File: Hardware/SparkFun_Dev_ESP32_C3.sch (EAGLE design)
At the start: 35 parts, among them J1 USB Female Type C Connector, J4 QWIIC_RIGHT_ANGLE, U1 ESP32-C3, U2 RT9080-33GJ5, U3 WS2812-2020, Y1 40MHZ

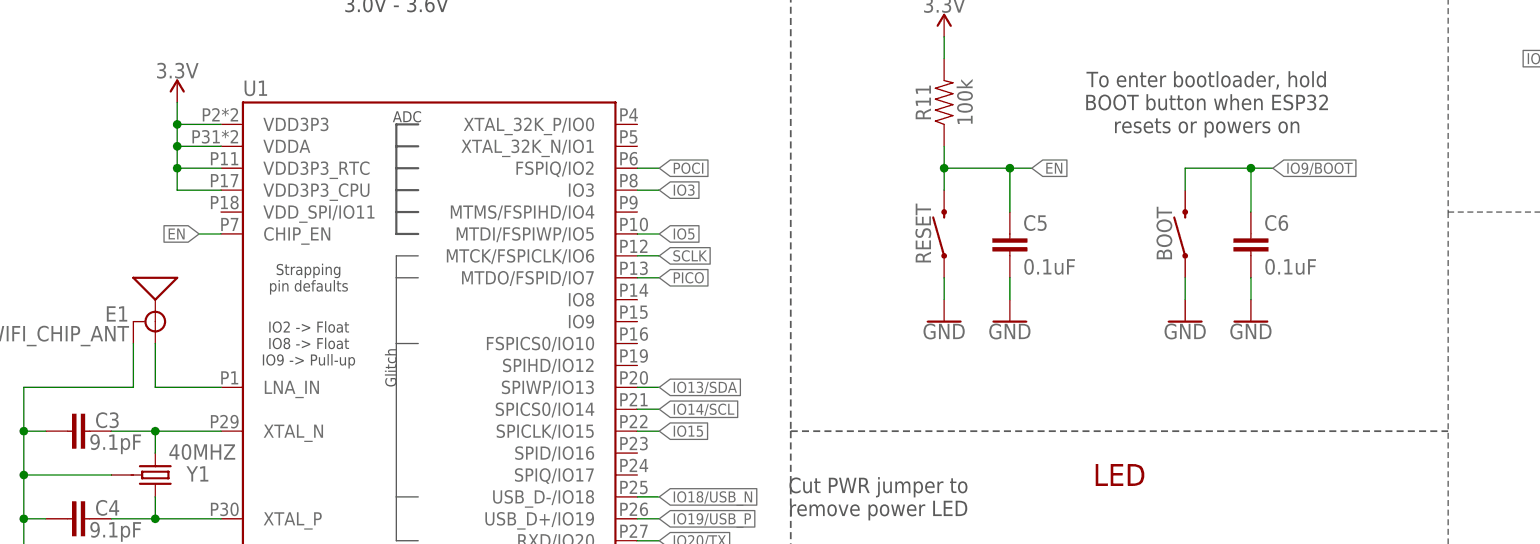
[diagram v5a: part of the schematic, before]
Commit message: Moves the parts into position
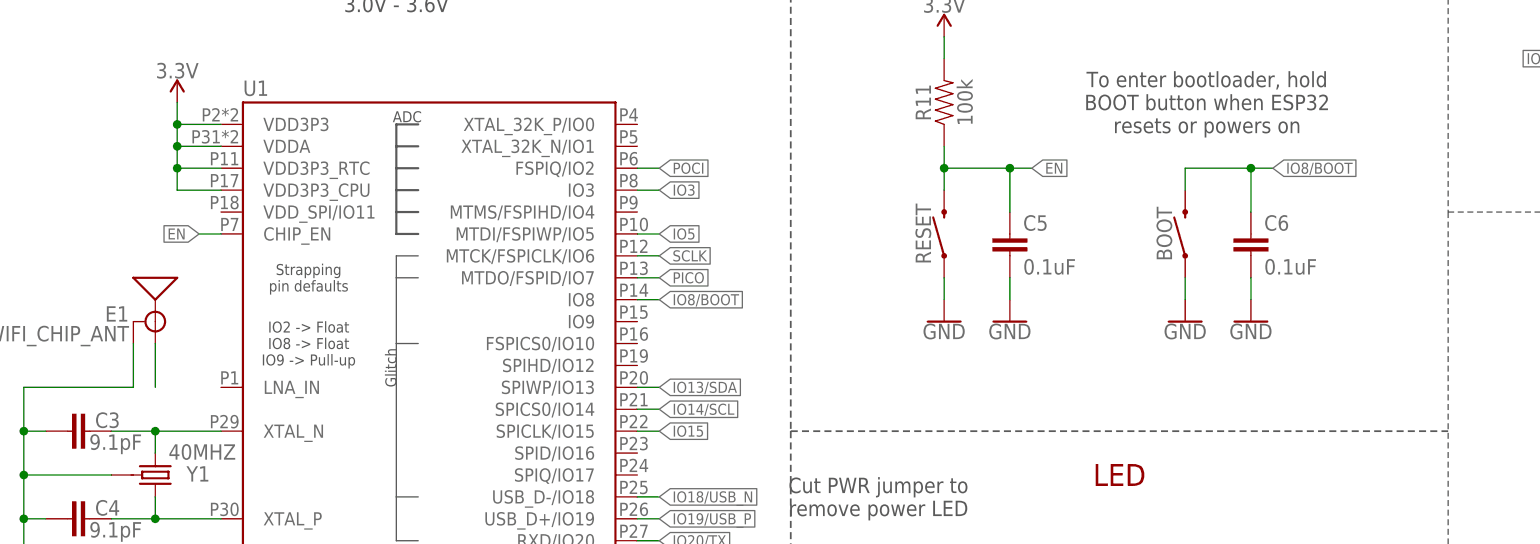
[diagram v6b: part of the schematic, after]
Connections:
- removed net IO9/BOOT: BOOT.2, C6.1
- removed net N$11: E1.SIGNAL, U1.LNA_IN
- new net ANT: E1.SIGNAL
- new net IO8/BOOT: BOOT.2, C6.1, U1.IO8
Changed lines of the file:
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@@
 </segment>
 </net>
-<net name="IO9/BOOT" class="0">
+<net name="IO8/BOOT" class="0">
 <segment>
 <pinref part="C6" gate="G$1" pin="1"/>
@@
 <junction x="533.4" y="129.54"/>
 <label x="535.94" y="129.54" size="1.27" layer="95" font="vector" xref="yes"/>
+</segment>
+<segment>
+<pinref part="U1" gate="G$1" pin="IO8"/>
+<wire x1="464.82" y1="114.3" x2="462.28" y2="114.3" width="0.1524" layer="91"/>
+<label x="464.82" y="114.3" size="1.27" layer="95" font="vector" xref="yes"/>
 </segment>
 </net>
@@
 </segment>
 </net>
-<net name="N$11" class="0">
+<net name="ANT" class="0">
 <segment>
 <wire x1="406.4" y1="104.14" x2="406.4" y2="109.22" width="0.1524" layer="91"/>
-<pinref part="U1" gate="G$1" pin="LNA_IN"/>
-<wire x1="406.4" y1="104.14" x2="414.02" y2="104.14" width="0.1524" layer="91"/>
 <pinref part="E1" gate="G$1" pin="SIGNAL"/>
 </segment>

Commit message: Fixes schematic
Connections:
- removed net GND1: JP14.4
- removed net RP_D+: JP14.3
- removed net RP_D-: JP14.2
- net GND: now also JP14.4
- net IO18/USB_N: now also JP14.2
- net IO19/USB_P: now also JP14.3
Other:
- moved on the sheet: BOOT, C1, C2, C3, C4, C5, C6, C7, C8, C9, D1, E1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

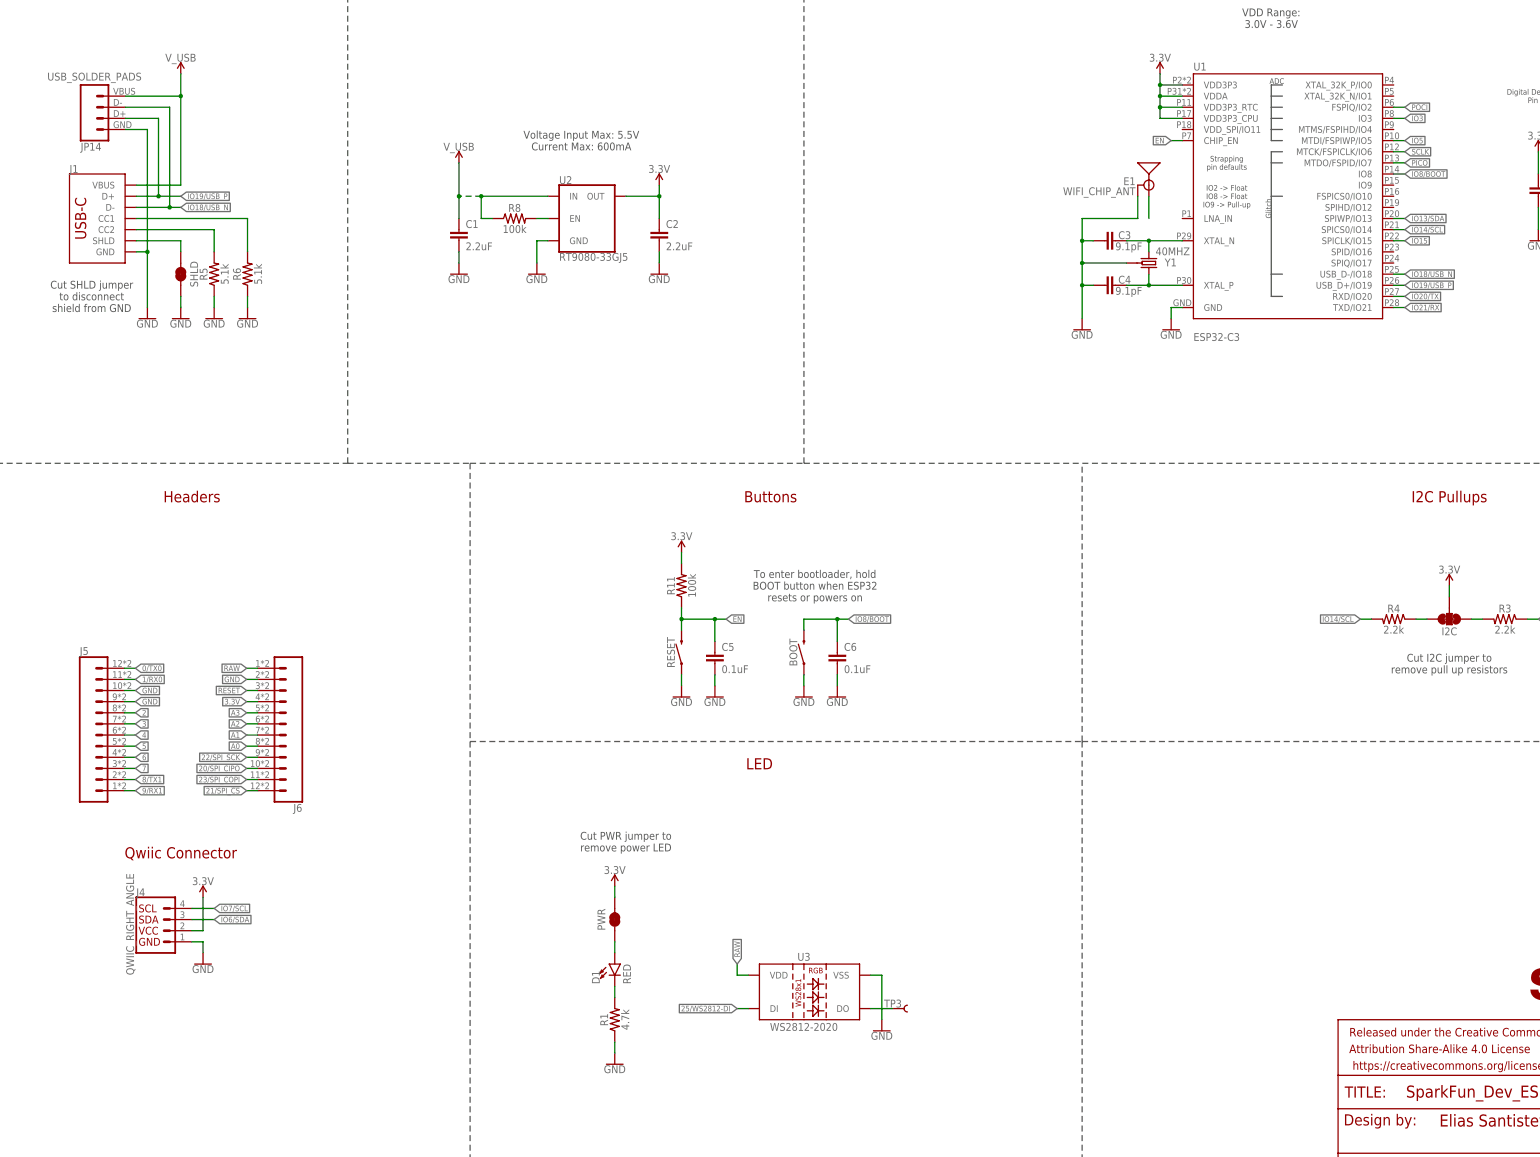
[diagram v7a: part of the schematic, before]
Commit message: More I/O netting from ESP32C3 to headers
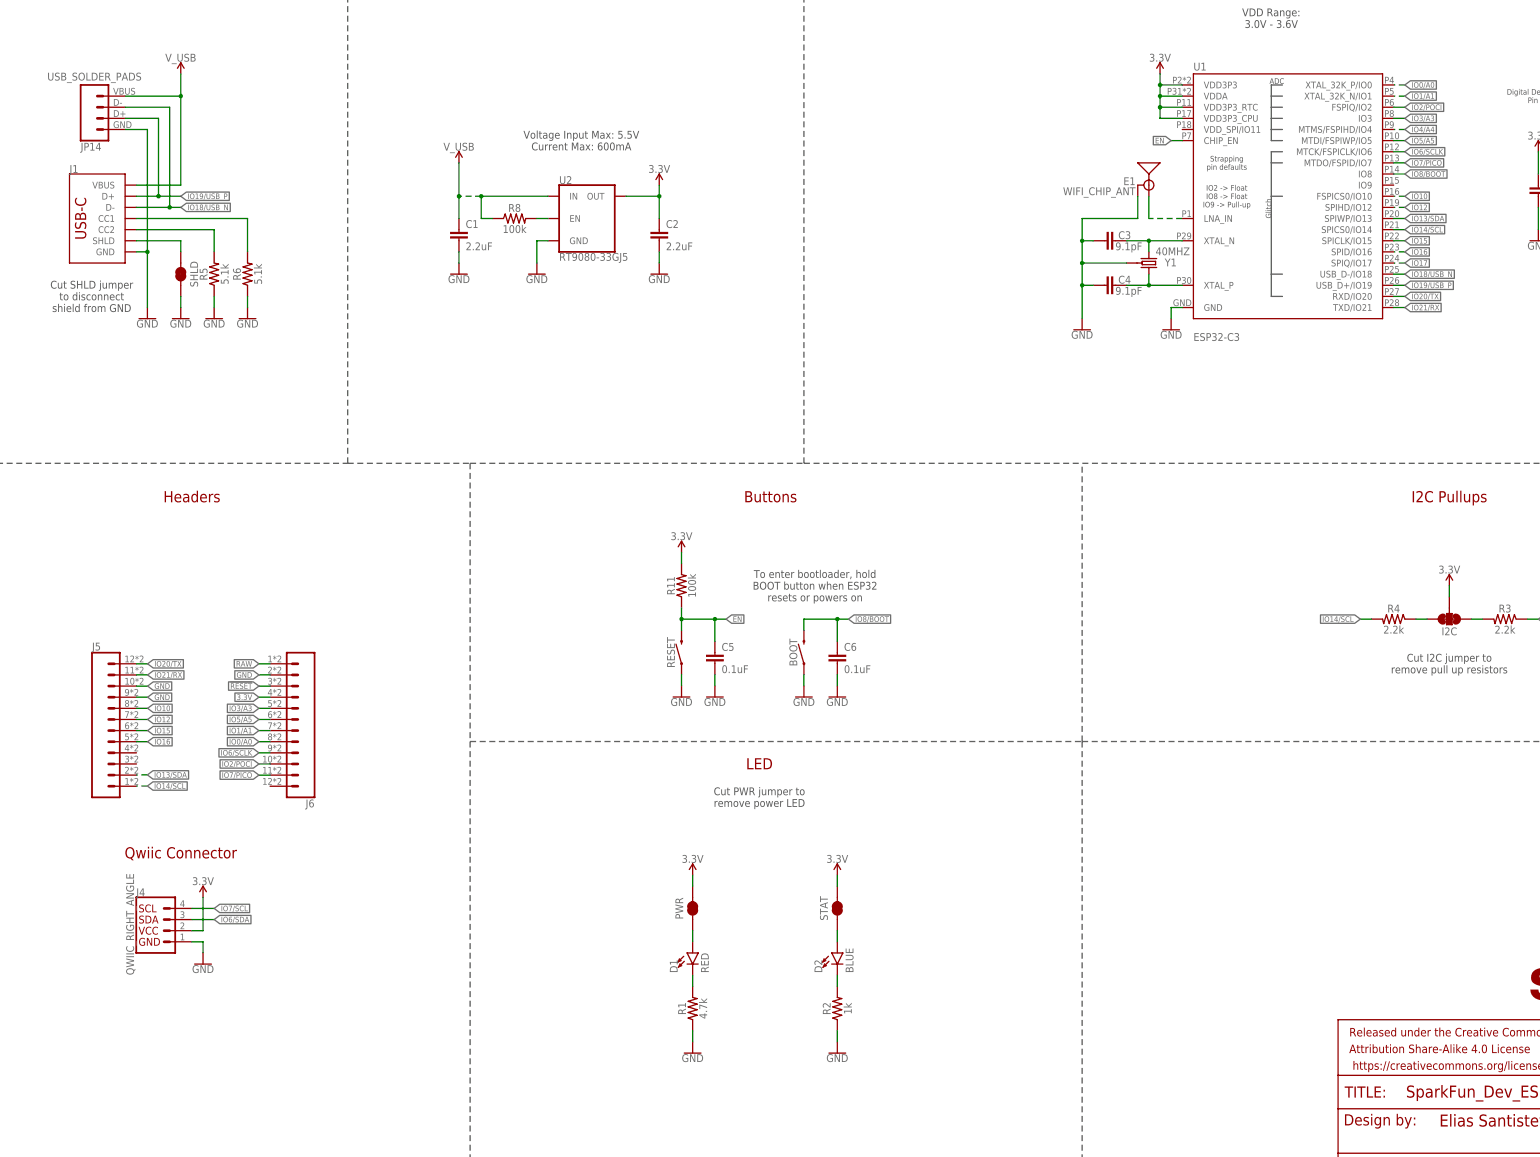
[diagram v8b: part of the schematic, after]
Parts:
- removed TP3: TEST-POINT3X5, SparkFun-Connectors:TEST-POINT3X5
- removed U3: WS2812-2020, SparkFun-LED:WS2812-2020
- added D2: BLUE, SparkFun-LED:LED-BLUE0603
- added R2: 1k, SparkFun-Resistors:1KOHM-0402T-1/16W-1%
- added STAT: JUMPER-SMT_2_NC_TRACE_SILK, SparkFun-Jumpers:JUMPER-SMT_2_NC_TRACE_SILK
- D1: device SparkFun-LED:LED-RED_0402 -> SparkFun-LED:LED-RED_0603-KB
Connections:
- removed net 0/TX0: J5.12
- removed net 1/RX0: J5.11
- removed net 2: J5.8
- removed net 20/SPI_CIPO: J6.10
- removed net 21/SPI_!CS!: J6.12
- removed net 22/SPI_SCK: J6.9
- removed net 23/SPI_COPI: J6.11
- removed net 25/WS2812-DI: U3.DI
- removed net 3: J5.7
- removed net 4: J5.6
- removed net 5: J5.5
- removed net 6: J5.4
- removed net 7: J5.3
- removed net 8/TX1: J5.2
- removed net 9/RX1: J5.1
- removed net A0: J6.8
- removed net A1: J6.7
- removed net A2: J6.6
- removed net A3: J6.5
- removed net IO3: U1.IO3
- removed net IO5: U1.MTDI/FSPIWP/IO5
- removed net PICO: U1.MTDO/FSPID/IO7
- removed net POCI: U1.FSPIQ/IO2
- removed net SCLK: U1.MTCK/FSPICLK/IO6
- new net IO0/A0: J6.8, U1.XTAL_32K_P/IO0
- new net IO1/A1: J6.7, U1.XTAL_32K_N/IO1
- new net IO10: J5.8, U1.FSPICS0/IO10
- new net IO12: J5.7, U1.SPIHD/IO12
- new net IO16: J5.5, U1.SPID/IO16
- new net IO17: U1.SPIQ/IO17
- new net IO2/POCI: J6.10, U1.FSPIQ/IO2
- new net IO3/A3: J6.5, U1.IO3
- new net IO4/A4: U1.MTMS/FSPIHD/IO4
- new net IO5/A5: J6.6, U1.MTDI/FSPIWP/IO5
- new net IO6/SCLK: J6.9, U1.MTCK/FSPICLK/IO6
- new net IO7/PICO: J6.11, U1.MTDO/FSPID/IO7
- new net N$11: D2.A, STAT.1
- net 3.3V: now also STAT.2
- net ANT: now also U1.LNA_IN
- net GND: now also R2.1; no longer U3.VSS
- net IO13/SDA: now also J5.2
- net IO14/SCL: now also J5.1
- net IO15: now also J5.6
- net IO20/TX: now also J5.12
- net IO21/RX: now also J5.11
- net N$3: now also D2.C, R2.2; no longer TP3.1, U3.DO
- net RAW: no longer U3.VDD
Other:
- moved on the sheet: D1, J5, J6, PWR, R1
